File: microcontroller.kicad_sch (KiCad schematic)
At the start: 48 parts, among them SW1 TS-1010A-B, SW2 SK-3296S-01-L3, U1 STM32H743IIKx, U13 TJA1051TK-3, U2 TJA1051TK-3, U3 FM25CL64B, Y1 X50328MSB2GI

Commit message: Menyesuaikan Decoupling Cap, PullUp Resistor pada FM25CL64B, menambahkan RST Debugger.
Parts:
- added C44: 1u, Capacitor_SMD:C_0603_1608Metric, symbol Device:C
- added C45: 100n, Capacitor_SMD:C_0402_1005Metric, symbol Device:C
- added R72, R73, R74: 10k, symbol Device:R
- R4, R5: value 330 -> 1.5k
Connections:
- net +3V3_FMU: now also C44.1, C45.1, R72.1, R73.1, R74.1
- net GND: now also C44.2, C45.2
- net at U1.A1 (PE3), U3.7 (~{HOLD}): now also R73.2
- net at U1.A3 (PE1), U3.1 (~{CS}): now also R72.2
- net at U1.B1 (PE4), U3.3 (~{WP}): now also R74.2
- net NRST: now reaches C18.2, SW1.2, U1.J1 (NRST)
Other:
- note added: "13 VDD -> 100nF x 13; 4.7uF VREF+ -> 100nF; 1uF VDDA+ -> 100nF; 1uF"
- note added: "PC13 / PC14: open-drain output Active Low"

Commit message: Schematic Changes on MPN and Footprint
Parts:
- R4, R5: value 1.5k -> 1k5; MPN 0402WGF3300TCE -> 0402WGF1501TCE
- R72, R73, R74: footprint (none) -> Resistor_SMD:R_0402_1005Metric; MPN (none) -> 0402WGF1002TCE
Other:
- note added: "13 VDD → 100nF x 13; 4.7uF VREF+ VDDA+ → 100nF; 1uF VDD33_USB → 100nF"
- note removed: "13 VDD -> 100nF x 13; 4.7uF VREF+ -> 100nF; 1uF VDDA+ -> 100nF; 1uF"
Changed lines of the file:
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@@
 		)
 	)
-	(text "13 VDD -> 100nF x 13; 4.7uF\nVREF+ -> 100nF; 1uF\nVDDA+ -> 100nF; 1uF"
+	(text "13 VDD → 100nF x 13; 4.7uF\nVREF+ VDDA+ → 100nF; 1uF\nVDD33_USB → 100nF"
 		(exclude_from_sim no)
 		(at 36.576 42.672 0)
@@
 			)
 		)
-		(property "Value" "1.5k"
+		(property "Value" "1k5"
 			(at 108.966 132.334 0)
 			(show_name no)
@@
 			)
 		)
-		(property "MPN" "0402WGF3300TCE"
+		(property "MPN" "0402WGF1501TCE"
 			(at 105.41 130.81 0)
 			(hide yes)
@@
 			)
 		)
-		(property "Footprint" ""
+		(property "Footprint" "Resistor_SMD:R_0402_1005Metric"
 			(at 319.532 220.98 90)
 			(hide yes)
@@
 			)
 		)
+		(property "MPN" "0402WGF1002TCE"
+			(at 321.31 220.98 0)
+			(hide yes)
+			(show_name no)
+			(do_not_autoplace no)
+			(effects
+				(font
+					(size 1.27 1.27)
+				)
+			)
+		)
 		(pin "2"
 		)
@@
 			)
 		)
-		(property "Datasheet" "https://www.infineon.com/dgdl/Infineon-FM25V05_512-Kbit_(64_K_8)_Serial_(SPI)_F-RAM-DataSheet-v09_00-EN.pdf"
+		(property "Datasheet" "https://www.infineon.com/assets/row/public/documents/10/49/infineon-fm25cl64b-64-kbit-8-k-8-serial-spi-f-ram-datasheet-en.pdf?fileId=8ac78c8c7d0d8da4017d0ebdfcd83119"
 			(at 307.34 225.298 0)
 			(hide yes)
@@
 			)
 		)
-		(property "Footprint" ""
+		(property "Footprint" "Resistor_SMD:R_0402_1005Metric"
 			(at 328.422 220.98 90)
 			(hide yes)
@@
 			)
 		)
+		(property "MPN" "0402WGF1002TCE"
+			(at 330.2 220.98 0)
+			(hide yes)
+			(show_name no)
+			(do_not_autoplace no)
+			(effects
+				(font
+					(size 1.27 1.27)
+				)
+			)
+		)
 		(pin "2"
 		)
@@
 			)
 		)
-		(property "Value" "1.5k"
+		(property "Value" "1k5"
 			(at 98.806 132.334 0)
 			(show_name no)
@@
 			)
 		)
-		(property "MPN" "0402WGF3300TCE"
+		(property "MPN" "0402WGF1501TCE"
 			(at 95.25 130.81 0)
 			(hide yes)
@@
 			)
 		)
-		(property "Footprint" ""
+		(property "Footprint" "Resistor_SMD:R_0402_1005Metric"
 			(at 286.512 220.98 90)
 			(hide yes)
@@
 			(at 288.29 220.98 0)
 			(hide yes)
+			(show_name no)
+			(do_not_autoplace no)
+			(effects
+				(font
+					(size 1.27 1.27)
+				)
+			)
+		)
+		(property "MPN" "0402WGF1002TCE"
+			(at 288.29 220.98 0)
+			(hide yes)

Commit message: Mulai layout
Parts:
- R71: now not fitted
- U1: value STM32H743IIKx -> STM32H743IIK6
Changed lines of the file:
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@@
 			)
 		)
-		(property "Value" "STM32H743IIKx"
+		(property "Value" "STM32H743IIK6"
 			(at 226.9841 269.24 0)
 			(show_name no)
@@
 		(on_board yes)
 		(in_pos_files yes)
-		(dnp no)
+		(dnp yes)
 		(fields_autoplaced yes)
 		(property "Reference" "R71"

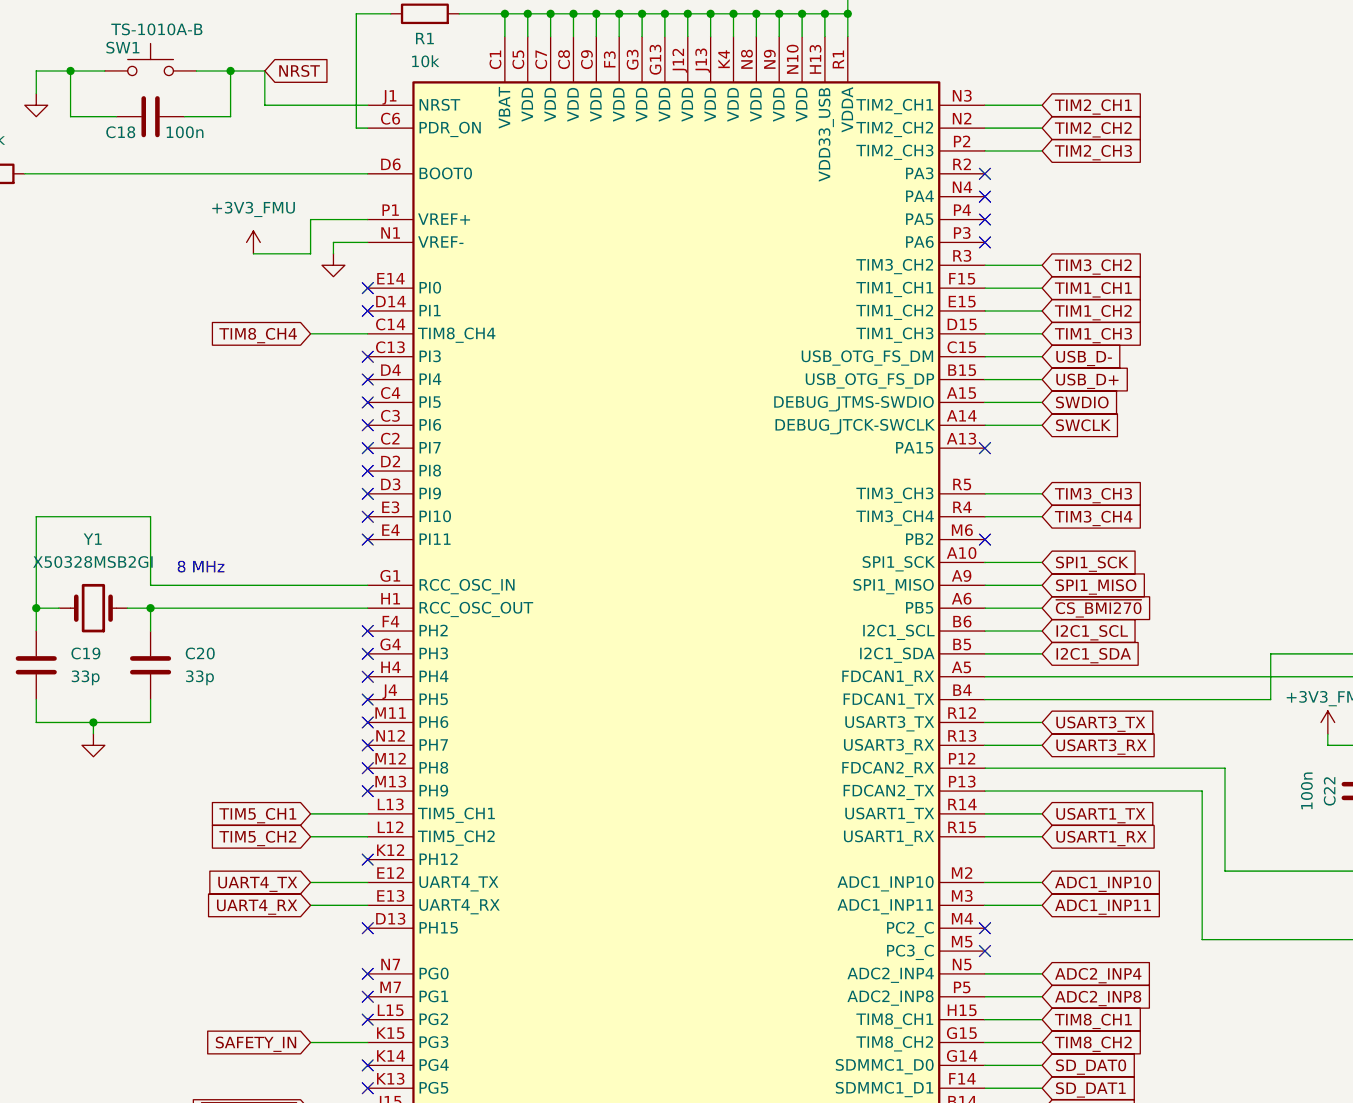
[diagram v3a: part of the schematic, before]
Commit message: Schematic: sensor redundancy + blok current limiter GPS (terverifikasi)
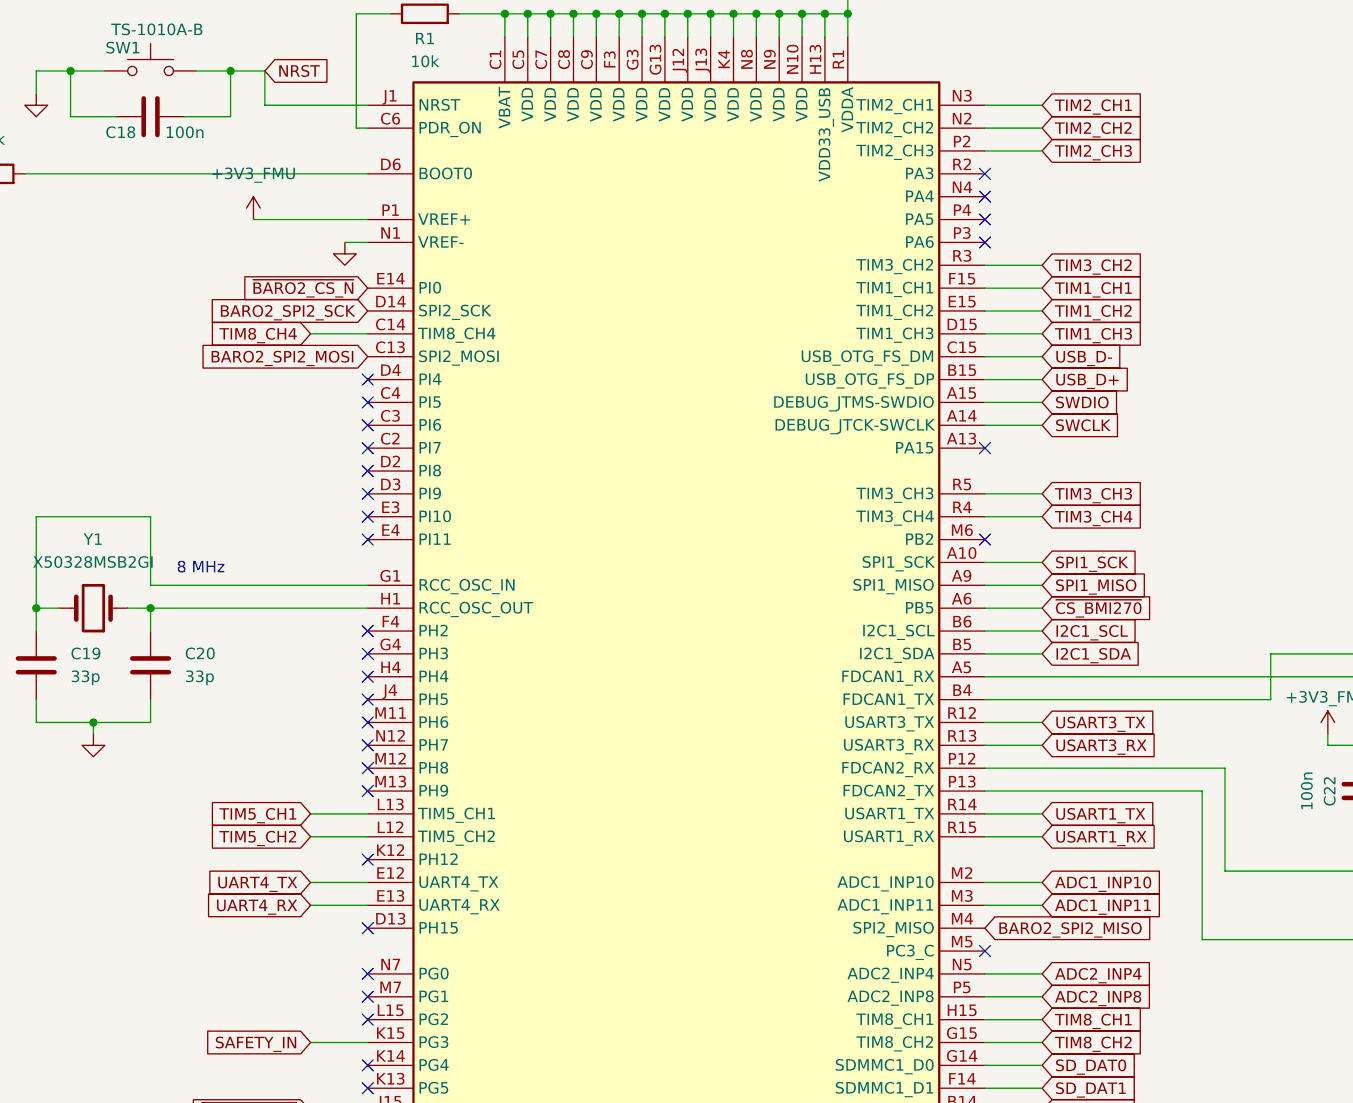
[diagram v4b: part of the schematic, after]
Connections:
- net BARO2_SPI2_MOSI: now reaches U1.C13 (PI3)
- net BARO2_SPI2_SCK: now reaches U1.D14 (PI1)
- net ~{BARO2_CS_N}: now reaches U1.E14 (PI0)
- net BARO2_SPI2_MISO: now reaches U1.M4 (PC2_C)
- no-connect marks 53 -> 49
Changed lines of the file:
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@@
 	)
 	(no_connect
-		(at 189.23 68.58)
-	)
-	(no_connect
 		(at 189.23 157.48)
 	)
@@
 	)
 	(no_connect
-		(at 189.23 76.2)
-	)
-	(no_connect
 		(at 257.81 142.24)
 	)
@@
 	)
 	(no_connect
-		(at 257.81 139.7)
-	)
-	(no_connect
 		(at 257.81 251.46)
 	)
@@
 	)
 	(no_connect
-		(at 189.23 71.12)
-	)
-	(no_connect
 		(at 257.81 60.96)
 	)
@@
 	(wire
 		(pts
-			(xy 185.42 64.77) (xy 185.42 63.5)
-		)
-		(stroke
-			(width 0)
-			(type default)
-		)
-	)
-	(wire
-		(pts
 			(xy 222.25 38.1) (xy 222.25 40.64)
 		)
@@
 	(wire
 		(pts
-			(xy 182.88 60.96) (xy 189.23 60.96)
-		)
-		(stroke
-			(width 0)
-			(type default)
-		)
-	)
-	(wire
-		(pts
 			(xy 138.43 55.88) (xy 143.51 55.88)
 		)
@@
 	(wire
 		(pts
-			(xy 176.53 64.77) (xy 182.88 64.77)
+			(xy 176.53 60.96) (xy 189.23 60.96)
 		)
 		(stroke
@@
 	(wire
 		(pts
-			(xy 185.42 63.5) (xy 189.23 63.5)
+			(xy 186.69 63.5) (xy 189.23 63.5)
 		)
 		(stroke
@@
 	(wire
 		(pts
-			(xy 182.88 64.77) (xy 182.88 60.96)
-		)
-		(stroke
-			(width 0)
-			(type default)
-		)
-	)
-	(wire
-		(pts
 			(xy 369.57 154.94) (xy 369.57 153.67)
 		)
@@
 		)
 	)
+	(global_label "BARO2_SPI2_SCK"
+		(shape input)
+		(at 189.23 71.12 180)
+		(fields_autoplaced yes)
+		(effects
+			(font
+				(size 1.27 1.27)
+			)
+			(justify right)
+		)
+		(property "Intersheetrefs" "${INTERSHEET_REFS}"
+			(at 170.0977 71.12 0)
+			(hide yes)
+			(show_name no)
+			(do_not_autoplace no)
+			(effects
+				(font
+					(size 1.27 1.27)
+				)
+				(justify right)
+			)
+		)
+	)
 	(global_label "TIM2_CH3"
 		(shape input)
@@
 		)
 	)
+	(global_label "~{BARO2_CS_N}"
+		(shape input)
+		(at 189.23 68.58 180)
+		(fields_autoplaced yes)
+		(effects
+			(font
+				(size 1.27 1.27)
+			)
+			(justify right)
+		)
+		(property "Intersheetrefs" "${INTERSHEET_REFS}"
+			(at 174.331 68.58 0)
+			(hide yes)
+			(show_name no)
+			(do_not_autoplace no)
+			(effects
+				(font
+					(size 1.27 1.27)
+				)
+				(justify right)
+			)
+		)
+	)
 	(global_label "~{CS_EXT1}"
 		(shape input)
@@
 		)
 	)
+	(global_label "BARO2_SPI2_MOSI"
+		(shape input)
+		(at 189.23 76.2 180)
+		(fields_autoplaced yes)
+		(effects
+			(font
+				(size 1.27 1.27)
+			)
+			(justify right)
+		)
+		(property "Intersheetrefs" "${INTERSHEET_REFS}"
+			(at 169.251 76.2 0)
+			(hide yes)
+			(show_name no)
+			(do_not_autoplace no)
+			(effects
+				(font
+					(size 1.27 1.27)
+				)
+				(justify right)
+			)
+		)
+	)
 	(global_label "SWCLK"
 		(shape input)
@@
 		)
 	)
+	(global_label "BARO2_SPI2_MISO"
+		(shape input)
+		(at 257.81 139.7 0)
+		(fields_autoplaced yes)
+		(effects
+			(font
+				(size 1.27 1.27)
+			)
+			(justify left)
+		)
+		(property "Intersheetrefs" "${INTERSHEET_REFS}"
+			(at 277.789 139.7 0)
+			(hide yes)
+			(show_name no)
+			(do_not_autoplace no)
+			(effects
+				(font
+					(size 1.27 1.27)
+				)
+				(justify left)
+			)
+		)
+	)
 	(global_label "SPI6_MISO"
 		(shape input)
@@
 		)
 		(pin "M4"
+			(alternate "SPI2_MISO")
 		)
 		(pin "M3"
@@
 		)
 		(pin "C13"
+			(alternate "SPI2_MOSI")
 		)
 		(pin "B1"
@@
 		)
 		(pin "D14"
+			(alternate "SPI2_SCK")
 		)
 		(pin "E2"
@@
 	)
 	(symbol
+		(lib_name "LED_2")
 		(lib_id "Device:LED")
 		(at 105.41 121.92 90)
@@
 	)
 	(symbol
+		(lib_name "TJA1051TK-3_1")
 		(lib_id "Interface_CAN_LIN:TJA1051TK-3")
 		(at 367.03 143.51 0)
@@
 	(symbol
 		(lib_id "power:+3V3")
-		(at 176.53 64.77 0)
+		(at 176.53 60.96 0)
 		(unit 1)
 		(body_style 1)
@@
 		(dnp no)
 		(property "Reference" "#PWR06"
-			(at 176.53 68.58 0)
+			(at 176.53 64.77 0)
 			(hide yes)
 			(show_name no)
@@
 		)
 		(property "Value" "+3V3_FMU"
-			(at 176.53 59.69 0)
+			(at 176.53 55.88 0)
 			(show_name no)
 			(do_not_autoplace no)
@@
 		)
 		(property "Footprint" ""
-			(at 176.53 64.77 0)
+			(at 176.53 60.96 0)
 			(hide yes)
 			(show_name no)
@@
 		)
 		(property "Datasheet" ""
-			(at 176.53 64.77 0)
+			(at 176.53 60.96 0)
 			(hide yes)
 			(show_name no)
@@
 		)
 		(property "Description" "Power symbol creates a global label with name \"+3V3\""
-			(at 176.53 64.77 0)
+			(at 176.53 60.96 0)
 			(hide yes)
 			(show_name no)
@@
 	)
 	(symbol
+		(lib_name "LED_1")
 		(lib_id "Device:LED")
 		(at 85.09 121.92 90)
@@
 	(symbol
 		(lib_id "power:GND")
-		(at 185.42 64.77 0)
+		(at 186.69 63.5 0)
 		(unit 1)
 		(body_style 1)
@@
 		(fields_autoplaced yes)
 		(property "Reference" "#PWR07"
-			(at 185.42 71.12 0)
+			(at 186.69 69.85 0)
 			(hide yes)
 			(show_name no)
@@
 		)
 		(property "Value" "GND"
-			(at 185.42 69.85 0)
+			(at 186.69 68.58 0)
 			(hide yes)
 			(show_name no)
@@
 		)
 		(property "Footprint" ""
-			(at 185.42 64.77 0)
+			(at 186.69 63.5 0)
 			(hide yes)
 			(show_name no)
@@
 		)
 		(property "Datasheet" ""
-			(at 185.42 64.77 0)
+			(at 186.69 63.5 0)
 			(hide yes)
 			(show_name no)
@@
 		)
 		(property "Description" "Power symbol creates a global label with name \"GND\" , ground"
-			(at 185.42 64.77 0)
+			(at 186.69 63.5 0)
 			(hide yes)
 			(show_name no)

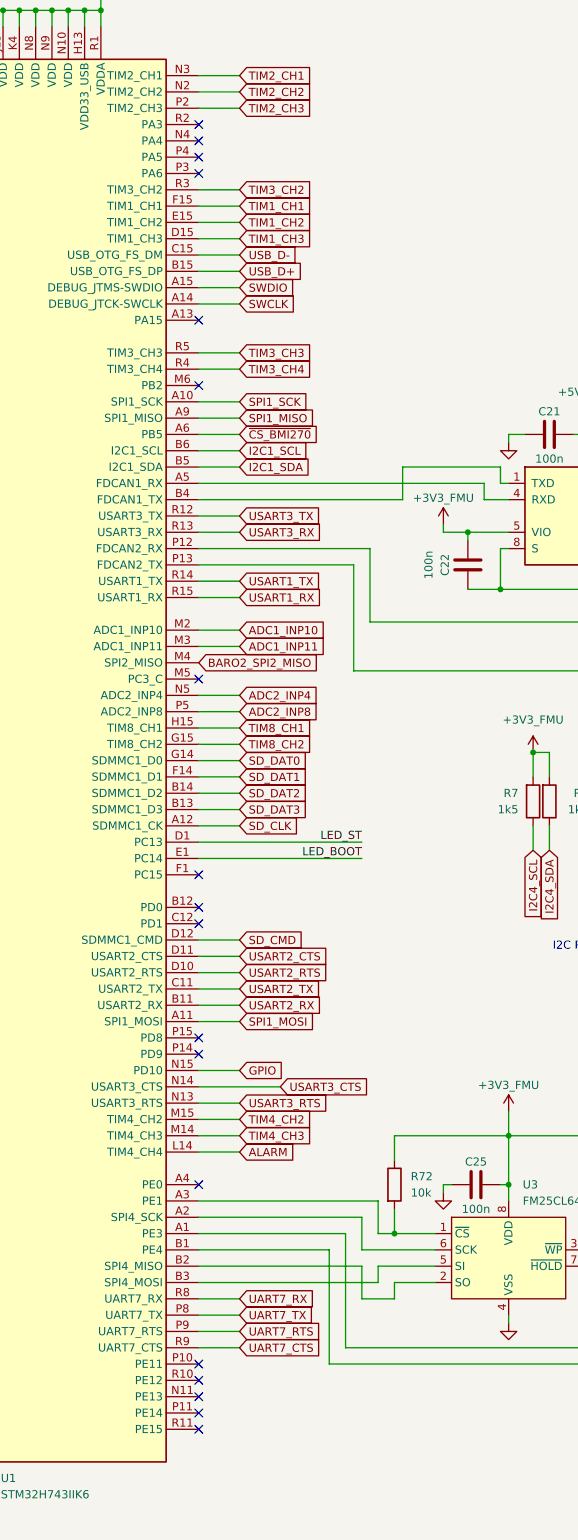
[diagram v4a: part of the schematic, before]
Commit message: Schematic: proteksi +VSERVO lengkap (TVS SMAJ6.0A + bulk + 16x1uF per-port) + konektor servo 3-pin + OC ke MCU; ERC 55 (verified)
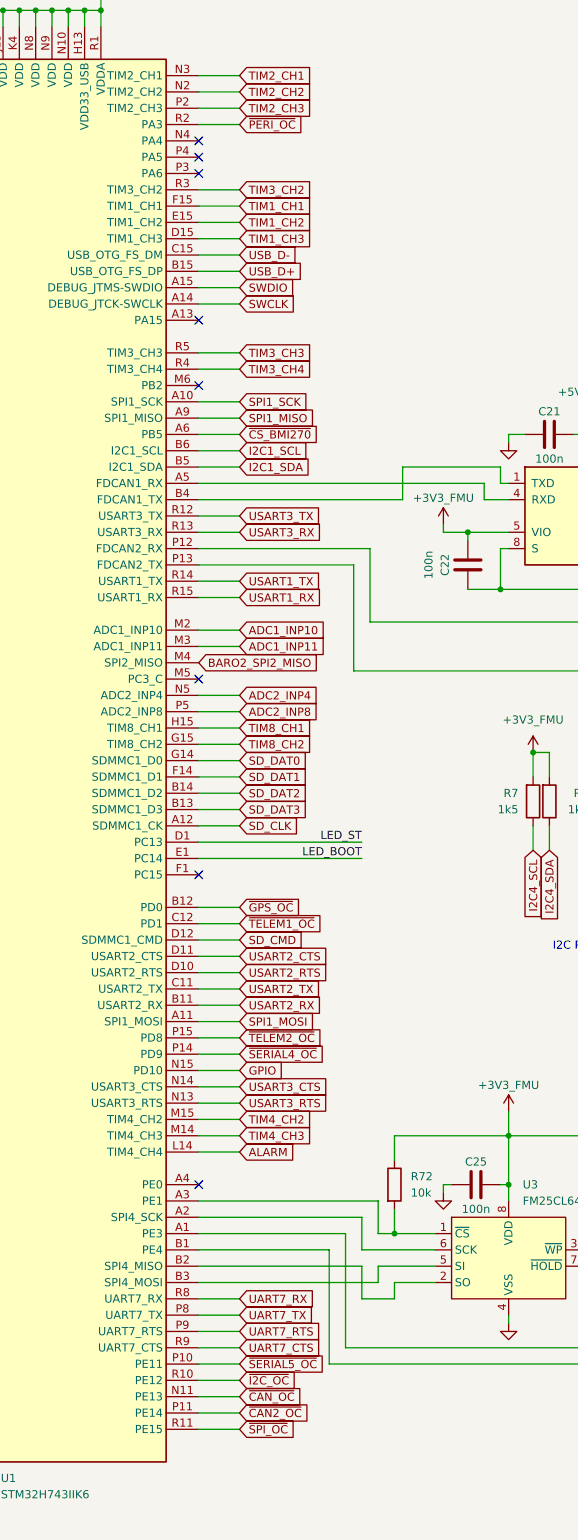
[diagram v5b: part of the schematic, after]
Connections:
- net ~{GPS_OC}: now reaches U1.B12 (PD0)
- net ~{TELEM1_OC}: now reaches U1.C12 (PD1)
- net ~{CAN_OC}: now reaches U1.N11 (PE13)
- net ~{SERIAL5_OC}: now reaches U1.P10 (PE11)
- net ~{CAN2_OC}: now reaches U1.P11 (PE14)
- net ~{SERIAL4_OC}: now reaches U1.P14 (PD9)
- net ~{TELEM2_OC}: now reaches U1.P15 (PD8)
- net ~{I2C_OC}: now reaches U1.R10 (PE12)
- net ~{SPI_OC}: now reaches U1.R11 (PE15)
- net ~{PERI_OC}: now reaches U1.R2 (PA3)
- no-connect marks 49 -> 39

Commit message: ERC: R80 DNP+100k+fp, Pin Conflicts Map lengkap; 0 errors / 17 lib-warnings (netlist diff 0, verified)
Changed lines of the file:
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@@
+	)
+	(symbol
+		(lib_id "power:PWR_FLAG")
+		(at 35.56 31.75 180)
+		(unit 1)
+		(body_style 1)
+		(exclude_from_sim no)
+		(in_bom yes)
+		(on_board yes)
+		(in_pos_files yes)
+		(dnp no)
+		(fields_autoplaced yes)
+		(property "Reference" "#FLG05"
+			(at 35.56 33.655 0)
+			(hide yes)
+			(show_name no)
+			(do_not_autoplace no)
+			(effects
+				(font
+					(size 1.27 1.27)
+				)
+			)
+		)
+		(property "Value" "PWR_FLAG"
+			(at 35.56 36.83 0)
+			(show_name no)
+			(do_not_autoplace no)
+			(effects
+				(font
+					(size 1.27 1.27)
+				)
+			)
+		)
+		(property "Footprint" ""
+			(at 35.56 31.75 0)
+			(hide yes)
+			(show_name no)
+			(do_not_autoplace no)
+			(effects
+				(font
+					(size 1.27 1.27)
+				)
+			)
+		)
+		(property "Datasheet" ""
+			(at 35.56 31.75 0)
+			(hide yes)
+			(show_name no)
+			(do_not_autoplace no)
+			(effects
+				(font
+					(size 1.27 1.27)
+				)
+			)
+		)
+		(property "Description" "Special symbol for telling ERC where power comes from"
+			(at 35.56 31.75 0)
+			(hide yes)
+			(show_name no)
+			(do_not_autoplace no)
+			(effects
+				(font
+					(size 1.27 1.27)
+				)
+			)
+		)
+		(pin "1"
+		)
+		(instances
+			(project "SvayamV3_IIK"
+				(path "/2845b085-eb04-41a1-8594-b2a880ca4ab0/b0345742-7dfd-4430-be6c-674e52a07160"
+					(reference "#FLG05")
+					(unit 1)
+				)
+			)
+		)
 	)
 	(symbol

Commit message: Annotate: renumber total semua ref (Entire+Reset+X) — netlist 1009 node identik, ERC 0E/17W
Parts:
- renumbered C44 to C1, C8 to C10, C9 to C11, C10 to C12, C19 to C13, C11 to C14, C18 to C15, C20 to C16, C23 to C17, C12 to C18, C24 to C19, C45 to C2, C13 to C20, C14 to C21, C15 to C22, C16 to C23, C17 to C24, C22 to C25, C25 to C26, C21 to C27, C42 to C28, C43 to C29, C1 to C3, C2 to C4, C3 to C5, C4 to C6, C5 to C7, C6 to C8, C7 to C9, R3 to R1, R9 to R10, R10 to R11, R74 to R12, R6 to R13, R71 to R14, R4 to R2, R5 to R3, R2 to R4, R1 to R5, R72 to R6, R73 to R9, SW2 to SW1, SW1 to SW2, U3 to U2, U2 to U3, U13 to U4
